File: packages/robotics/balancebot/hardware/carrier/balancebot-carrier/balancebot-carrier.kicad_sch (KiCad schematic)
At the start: 19 parts, among them J1 JST-XH pack in, J2 LM2596 module, J3 GY-521 MPU6050, J4 Motor left, J5 Motor right, U1 XIAO RP2350

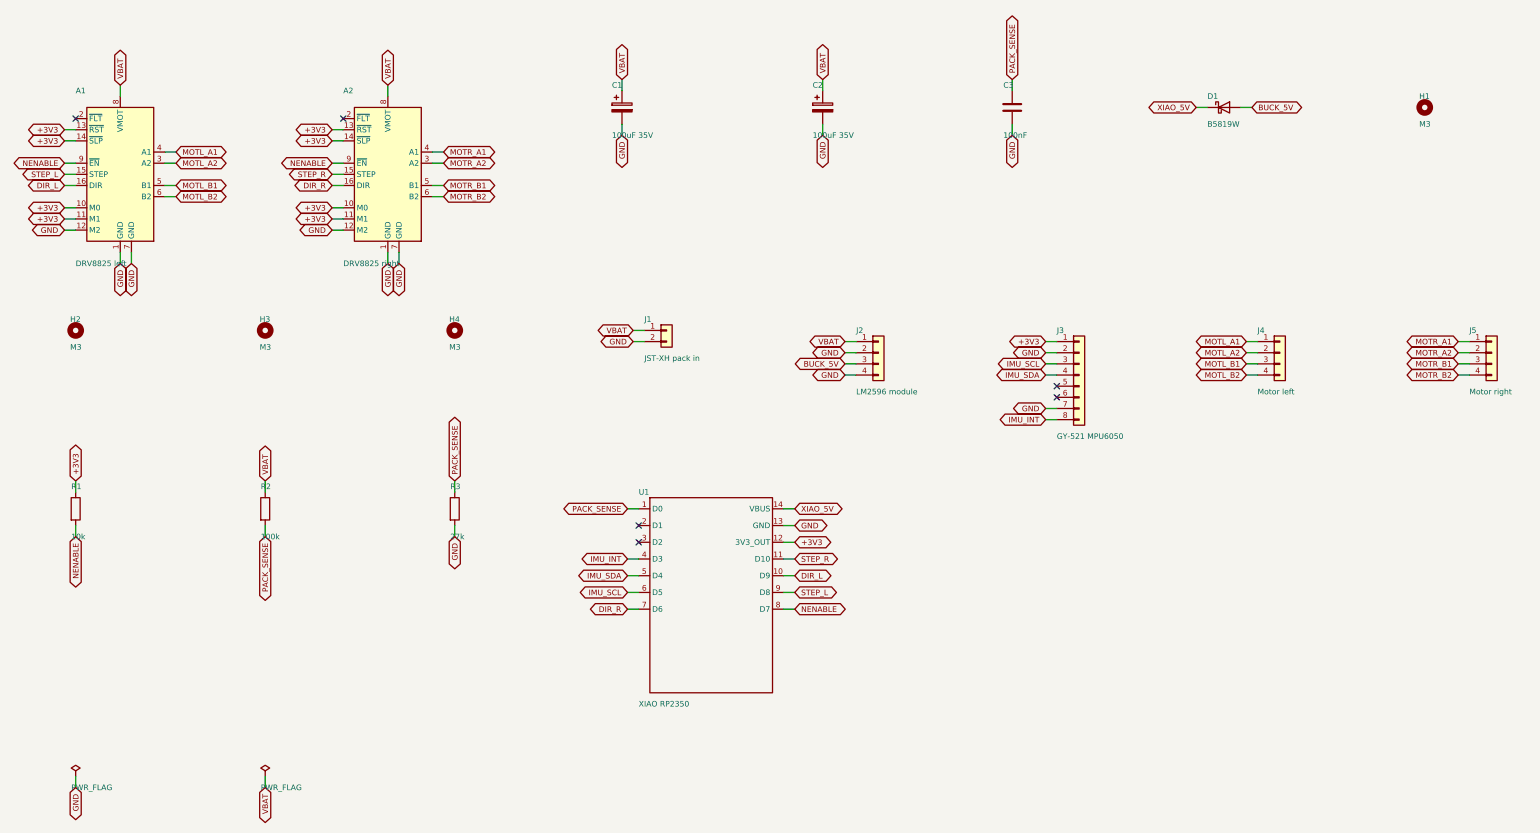
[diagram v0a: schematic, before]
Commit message: fix(balancebot): pre-order fixes to the carrier PCB
From the adversarial pre-order review:

- S1: VMOT, EN and DIR printed at the ends of each DRV8825 socket, since a
  Pololu-format module fits turned 180 degrees; README check "VMOT text =
  module's VMOT pin".
- S2: footprint silkscreen at 0.15 mm (was 0.10-0.127 mm), from the
  build_board.py floor; board-level "+" by C1 and C2 and "K" by D1.
- S3: J2 labelled IN+, -, 5V, - and J4/J5 A1, A2, B1, B2 by their pads;
  README: meter the buck lead before the first plug-in.
- S4: reverse-polarity and short protection at J1, as Lauri chose: F1 (3 A
  hold PTC, BSMD1812-300-24V) and Q1 (ZXMP4A16G P-MOSFET, drain to F1,
  source to VBAT, gate to GND through R4). Datasheet answers in the
  hardware.toml comment and the README. J1 turns 180 degrees so its BAT+
  pad faces F1; "+"/"-" move below it.
- N2: VBAT is fixed F.Cu tracks, 1.5 mm, with no via (was one 1.0/0.5 mm
  via in series to A2, C2 and R2 after 94 mm, and 30 mm of B.Cu).
- N4: C3 at the ADC pin, 2.3 mm from U1:1 (was 24.5 mm).
- N5: [fanout] vias at the SMD ground pads and [pour] stitch vias on a 5 mm
  grid: 118 GND vias (was 3).
- N6: a .kicad_dru rule keeps the pour 3.5 mm from each M3 hole's centre
  (was 1.85 mm, 0.25 mm from the hole).
- N1: README minimums measured on the routed board.
- N9: README notes the DRV8825's 8.2 V minimum and a ~9 V firmware cutoff
  (#747).

The perfboard layout gains F1, Q1 and R4 and a "Pack input" step.

Co-Authored-By: Claude Opus 5.5 <noreply@anthropic.com>
Claude-Session: https://claude.ai/code/session_01DgeoMcrSCUfJwedu77q6oo
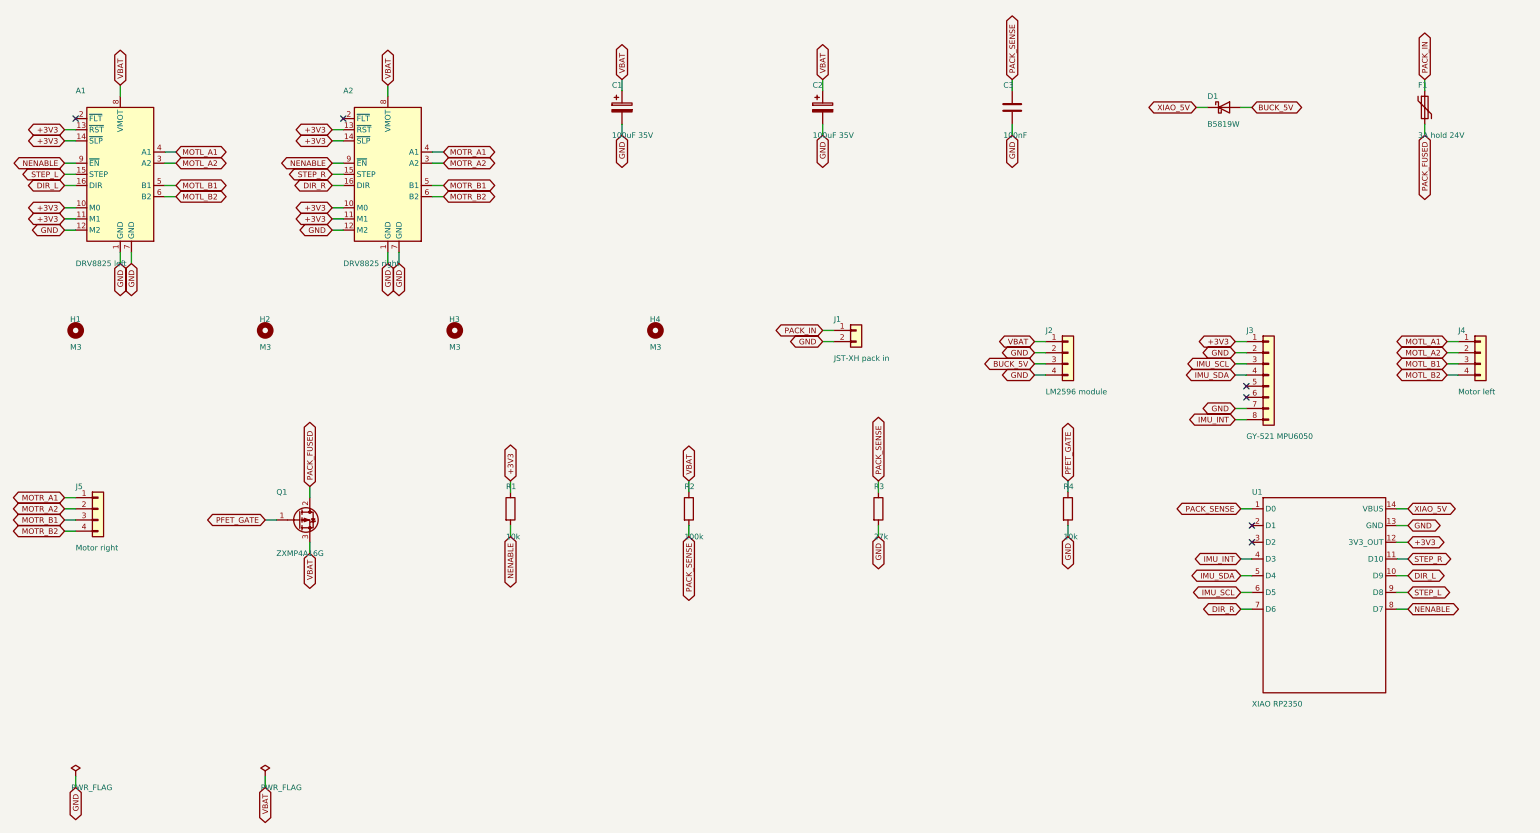
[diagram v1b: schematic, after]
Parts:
- added F1: 3A hold 24V, Fuse:Fuse_1812_4532Metric_Pad1.30x3.40mm_HandSolder, symbol Device:Polyfuse
- added Q1: ZXMP4A16G, Package_TO_SOT_SMD:SOT-223-3_TabPin2, symbol Transistor_FET:ZXMP4A16G
- added R4: 10k, Resistor_SMD:R_0805_2012Metric_Pad1.20x1.40mm_HandSolder, symbol Device:R
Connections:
- net GND: now also R4.2
- net VBAT: now also Q1.3 (S); no longer J1.1 (Pin_1)
- new net PACK_FUSED: F1.2, Q1.2 (D)
- new net PACK_IN: F1.1, J1.1 (Pin_1)
- new net PFET_GATE: Q1.1 (G), R4.1
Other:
- moved on the sheet: H1, H2, H3, H4, J1, J2, J3, J4, J5, R1, R2, R3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
